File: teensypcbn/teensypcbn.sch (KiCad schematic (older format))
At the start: 10 parts, among them J1 CONN_26X2, J2 CONN_26X2, U1 Teensy4.1

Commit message: schema
schema voledig klaar
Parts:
- removed T?: HX1198FNLT, HX1198FNLT, symbol SamacSys_Parts:HX1198FNLT
- added C5, C6: 1000pF, Capacitor_SMD:C_0603_1608Metric_Pad0.99x1.00mm_HandSolder, symbol ESP32-PoE-ISO_Rev_C:Cap_Small
- added J4: SS-7188S-A-NF, SamacSys_Parts:SS-7188S-A-NF, symbol SamacSys_Parts:SS-7188S-A-NF
- added R1, R2, R3, R4: R_US, Resistor_SMD:R_0603_1608Metric, symbol Device:R_US
- added T1: HX1198FNLT, SamacSys_Parts:HX1198FNLT, symbol SamacSys_Parts:HX1198FNLT
- C1, C2, C3, C4: renamed from C?; footprint (none) -> Capacitor_SMD:C_0603_1608Metric_Pad0.99x1.00mm_HandSolder
- J3: renamed from J?; footprint 629104190121 -> SamacSys_Parts:629104190121
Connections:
- net RN: now also T1.8
- net RP: now also T1.6
- net TN: now also T1.3
- net TP: now also T1.1
- net at C1.1, C2.2: now also T1.2
- net at C3.1, C4.2: now also T1.7
- new net: R1.1, T1.10
- new net: J4.3, T1.11
- new net: J4.2, T1.14
- new net: R2.1, T1.15
- new net: J4.1, T1.16
- new net: J4.6, T1.9
- new net: J4.4, J4.5, R3.1
- new net: J4.7, J4.8, R4.1
- new net: C6.1, R3.2, R4.2
- new net: C5.1, R1.2, R2.2
- new net Earth: C5.2, C6.2
- no-connect marks 4 -> 6

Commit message: routing
routing begonnen
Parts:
- BT1: footprint Connector_JST:JST_PH_S2B-PH-SM4-TB_1x02-1MP_P2.00mm_Horizontal -> Connector_JST:JST_PH_B2B-PH-SM4-TB_1x02-1MP_P2.00mm_Vertical
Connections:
- net Earth is gone; now on net GND: C5.2, C6.2
- net R1P: now reaches J4.3, T1.11
- net T1N: now reaches J4.2, T1.14
- net T1P: now reaches J4.1, T1.16
- net R1N: now reaches J4.6, T1.9
- net LED0: no longer names the net of U1.61 (LED)
- no-connect marks 6 -> 7
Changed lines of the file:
@@
 F 0 "BT1" V 3975 770 50  0000 C CNN
 F 1 "Battery" V 4066 770 50  0000 C CNN
-F 2 "Connector_JST:JST_PH_S2B-PH-SM4-TB_1x02-1MP_P2.00mm_Horizontal" V 4220 830 50  0001 C CNN
+F 2 "Connector_JST:JST_PH_B2B-PH-SM4-TB_1x02-1MP_P2.00mm_Vertical" V 4220 830 50  0001 C CNN
 F 3 "~" V 4220 830 50  0001 C CNN
 	1    4220 770
@@
 Wire Wire Line
 	7490 4770 7970 4770
-Wire Wire Line
-	6970 4470 7210 4470
 $Comp
 L ESP32-PoE-ISO_Rev_C:Cap_Small C1
@@
 NoConn ~ 7970 4470
 NoConn ~ 7970 4370
-Text Label 7210 4470 2    50   ~ 0
-LED0
 Text Label 7085 4070 0    50   ~ 0
 TP
@@
 	9650 5620 9650 5290
 Connection ~ 9775 5620
-$Comp
-L power:Earth #PWR0105
-U 1 1 5F11E832
-P 9775 5810
-F 0 "#PWR0105" H 9775 5560 50  0001 C CNN
-F 1 "Earth" H 9775 5660 50  0001 C CNN
-F 2 "" H 9775 5810 50  0001 C CNN
-F 3 "~" H 9775 5810 50  0001 C CNN
-	1    9775 5810
-	1    0    0    -1
-$EndComp
 Wire Wire Line
 	9775 5810 9775 5720
@@
 	8990 5725 8990 5395
 Connection ~ 9115 5725
-$Comp
-L power:Earth #PWR0106
-U 1 1 5F1344FD
-P 9115 5915
-F 0 "#PWR0106" H 9115 5665 50  0001 C CNN
-F 1 "Earth" H 9115 5765 50  0001 C CNN
-F 2 "" H 9115 5915 50  0001 C CNN
-F 3 "~" H 9115 5915 50  0001 C CNN
-	1    9115 5915
-	1    0    0    -1
-$EndComp
 Wire Wire Line
 	9115 5915 9115 5825
@@
 Wire Wire Line
 	9915 4370 9665 4370
+Text Label 9125 4070 0    50   ~ 0
+T1P
+Text Label 9090 4270 0    50   ~ 0
+T1N
+Text Label 9085 4570 0    50   ~ 0
+R1P
+Text Label 9060 4770 0    50   ~ 0
+R1N
+$Comp
+L power:GND #PWR0106
+U 1 1 5F06739F
+P 9775 5810
+F 0 "#PWR0106" H 9775 5560 50  0001 C CNN
+F 1 "GND" H 9780 5637 50  0000 C CNN
+F 2 "" H 9775 5810 50  0001 C CNN
+F 3 "" H 9775 5810 50  0001 C CNN
+	1    9775 5810
+	1    0    0    -1
+$EndComp
+$Comp
+L power:GND #PWR0105
+U 1 1 5F0429FF
+P 9115 5915
+F 0 "#PWR0105" H 9115 5665 50  0001 C CNN
+F 1 "GND" H 9120 5742 50  0000 C CNN
+F 2 "" H 9115 5915 50  0001 C CNN
+F 3 "" H 9115 5915 50  0001 C CNN
+	1    9115 5915
+	1    0    0    -1
+$EndComp
+NoConn ~ 6970 4470
 $EndSCHEMATC

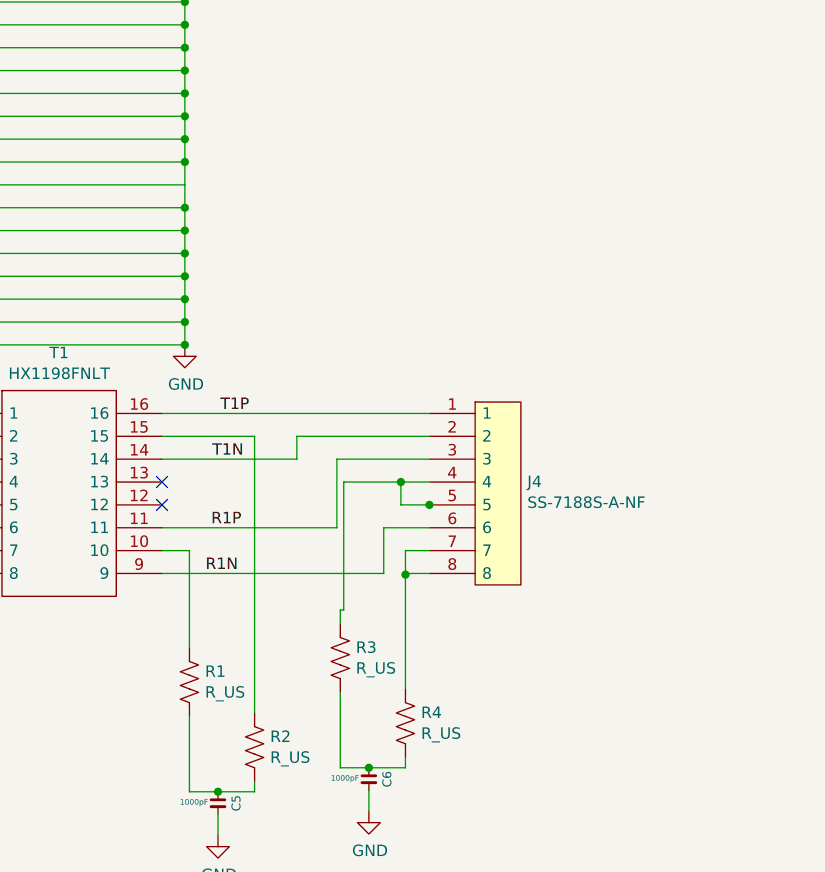
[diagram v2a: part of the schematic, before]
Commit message: routing V2
routing gestart met de juiste connector
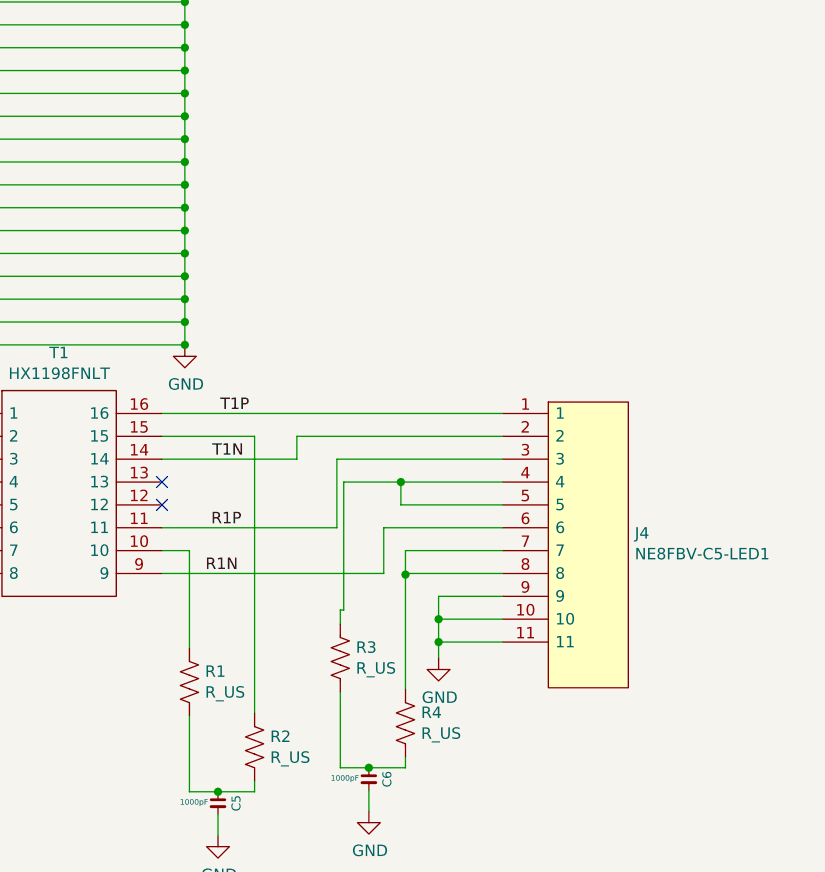
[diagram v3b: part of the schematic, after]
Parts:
- removed J4: SS-7188S-A-NF, SamacSys_Parts:SS-7188S-A-NF, symbol SamacSys_Parts:SS-7188S-A-NF
- added J4: NE8FBV-C5-LED1, SamacSys_Parts:NE8FBVC5LED1, symbol SamacSys_Parts:NE8FBV-C5-LED1
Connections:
- net GND: now also J2.15, J4.10, J4.11, J4.9
- net R1N: now also J4.6
- net R1P: now also J4.3
- net T1N: now also J4.2
- net T1P: now also J4.1
- net at R3.1: now also J4.4, J4.5
- net at R4.1: now also J4.7, J4.8
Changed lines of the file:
@@
 	8100 3170 8970 3170
 Wire Wire Line
-	8970 3270 8970 3170
-Connection ~ 8970 3170
-Wire Wire Line
 	8100 2970 8970 2970
-Wire Wire Line
-	8970 3170 8970 2970
-Connection ~ 8970 2970
 Wire Wire Line
 	8100 2870 8970 2870
@@
 Wire Wire Line
 	7970 4670 7970 4710
-$Comp
-L SamacSys_Parts:SS-7188S-A-NF J4
-U 1 1 5F04A257
-P 10240 4370
-F 0 "J4" H 10468 4371 50  0000 L CNN
-F 1 "SS-7188S-A-NF" H 10468 4280 50  0000 L CNN
-F 2 "SamacSys_Parts:SS-7188S-A-NF" H 10490 4620 50  0001 L CNN
-F 3 "" H 10490 4520 50  0001 L CNN
-F 4 "Bel-Stewart Cat5e RJ45 Connector Socket, Shielded, Right Angle, Through Hole" H 10490 4420 50  0001 L CNN "Description"
-F 5 "530-SS-7188S-A-NF" H 10490 4220 50  0001 L CNN "Mouser Part Number"
-F 6 "https://www.mouser.co.uk/ProductDetail/Stewart-Connector-Bel/SS-7188S-A-NF?qs=FESYatJ8odJ%252BI%2FN%2FnbWjsA%3D%3D" H 10490 4120 50  0001 L CNN "Mouser Price/Stock"
-F 7 "Bel-Stewart" H 10490 4020 50  0001 L CNN "Manufacturer_Name"
-F 8 "SS-7188S-A-NF" H 10490 3920 50  0001 L CNN "Manufacturer_Part_Number"
-	1    10240 4370
-	1    0    0    -1
-$EndComp
-Wire Wire Line
-	8870 4070 10040 4070
 Wire Wire Line
 	8870 4270 9460 4270
 Wire Wire Line
 	9460 4270 9460 4170
-Wire Wire Line
-	9460 4170 10040 4170
 NoConn ~ 8870 4370
 NoConn ~ 8870 4470
@@
 	9635 4570 9635 4270
 Wire Wire Line
-	9635 4270 10040 4270
-Wire Wire Line
 	8870 4770 9840 4770
 Wire Wire Line
 	9840 4770 9840 4570
-Wire Wire Line
-	9840 4570 10040 4570
 $Comp
 L Device:R_US R3
@@
 $EndComp
 Wire Wire Line
-	10040 4670 9935 4670
-Wire Wire Line
 	9935 4670 9935 4775
-Wire Wire Line
-	10040 4770 9940 4770
 Wire Wire Line
 	9940 4770 9940 4775
@@
 	9275 4170 9275 5380
 Wire Wire Line
-	10040 4370 9915 4370
-Wire Wire Line
 	9665 4370 9665 4930
 Wire Wire Line
@@
 	9650 4930 9650 4990
 Wire Wire Line
-	10045 4470 10040 4470
-Wire Wire Line
 	9915 4470 9915 4370
-Connection ~ 10040 4470
-Wire Wire Line
-	10040 4470 9915 4470
 Connection ~ 9915 4370
 Wire Wire Line
@@
 $EndComp
 NoConn ~ 6970 4470
+Wire Wire Line
+	8970 2970 8970 3070
+Connection ~ 8970 2970
+Wire Wire Line
+	8970 3070 8970 3170
+Connection ~ 8970 3070
+Connection ~ 8970 3170
+Wire Wire Line
+	8970 3170 8970 3270
+$Comp
+L power:GND #PWR0107
+U 1 1 5F0723BF
+P 10080 5140
+F 0 "#PWR0107" H 10080 4890 50  0001 C CNN
+F 1 "GND" H 10085 4967 50  0000 C CNN
+F 2 "" H 10080 5140 50  0001 C CNN
+F 3 "" H 10080 5140 50  0001 C CNN
+	1    10080 5140
+	1    0    0    -1
+$EndComp
+Wire Wire Line
+	9940 4770 10360 4770
+Wire Wire Line
+	9935 4670 10360 4670
+Wire Wire Line
+	8870 4070 10360 4070
+Wire Wire Line
+	9460 4170 10360 4170
+Wire Wire Line
+	9635 4270 10360 4270
+Wire Wire Line
+	9915 4370 10360 4370
+$Comp
+L SamacSys_Parts:NE8FBV-C5-LED1 J4
+U 1 1 5F0E1554
+P 10360 4070
+F 0 "J4" H 10938 3546 50  0000 L CNN
+F 1 "NE8FBV-C5-LED1" H 10938 3455 50  0000 L CNN
+F 2 "SamacSys_Parts:NE8FBVC5LED1" V 10860 3020 50  0001 L CNN
+F 3 "" H 9760 3520 50  0001 L CNN
+F 4 "28.7" H 10710 2920 50  0001 L CNN "Height"
+	1    10360 4070
+	1    0    0    -1
+$EndComp
+Wire Wire Line
+	9915 4470 10360 4470
+Wire Wire Line
+	9840 4570 10360 4570
+Wire Wire Line
+	10080 4870 10360 4870
+Wire Wire Line
+	10360 4970 10080 4970
+Connection ~ 10080 4970
+Wire Wire Line
+	10080 4970 10080 4870
+Wire Wire Line
+	10360 5070 10080 5070
+Wire Wire Line
+	10080 4970 10080 5070
+Connection ~ 10080 5070
+Wire Wire Line
+	10080 5070 10080 5140
 $EndSCHEMATC

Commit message: placment
placment bijna klaar
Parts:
- removed J4: NE8FBV-C5-LED1, SamacSys_Parts:NE8FBVC5LED1, symbol SamacSys_Parts:NE8FBV-C5-LED1
- added J4: NE8FAH-C5, SamacSys_Parts:NE8FAHC5, symbol SamacSys_Parts:NE8FAH-C5
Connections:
- net GND: now also J4.G1
- net R1N: now also J4.6
- net R1P: now also J4.3
- net T1N: now also J4.2
- net T1P: now also J4.1
- net at R3.1: now also J4.4, J4.5
- net at R4.1: now also J4.7, J4.8
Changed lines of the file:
@@
 Wire Wire Line
 	9915 4370 10360 4370
-$Comp
-L SamacSys_Parts:NE8FBV-C5-LED1 J4
-U 1 1 5F0E1554
-P 10360 4070
-F 0 "J4" H 10938 3546 50  0000 L CNN
-F 1 "NE8FBV-C5-LED1" H 10938 3455 50  0000 L CNN
-F 2 "SamacSys_Parts:NE8FBVC5LED1" V 10860 3020 50  0001 L CNN
-F 3 "" H 9760 3520 50  0001 L CNN
-F 4 "28.7" H 10710 2920 50  0001 L CNN "Height"
-	1    10360 4070
-	1    0    0    -1
-$EndComp
 Wire Wire Line
 	9915 4470 10360 4470
@@
 Wire Wire Line
 	10080 4870 10360 4870
+$Comp
+L SamacSys_Parts:NE8FAH-C5 J4
+U 1 1 5F148EB7
+P 10360 4070
+F 0 "J4" H 10738 3691 50  0000 L CNN
+F 1 "NE8FAH-C5" H 10738 3600 50  0000 L CNN
+F 2 "SamacSys_Parts:NE8FAHC5" H 10760 3320 50  0001 L CNN
+F 3 "https://www.neutrik.com/media/10049/download/ne8fah-c5-1.pdf?v=1" H 10760 3420 50  0001 L CNN
+F 4 "NEUTRIK - NE8FAH-C5 - CONNECTOR, RJ45, JACK, 8P8C, CAT5E" H 10760 3520 50  0001 L CNN "Description"
+F 5 "28.7" H 10510 3470 50  0001 L CNN "Height"
+F 6 "568-NE8FAH-C5" H 10760 3720 50  0001 L CNN "Mouser Part Number"
+F 7 "https://www.mouser.co.uk/ProductDetail/Neutrik/NE8FAH-C5?qs=yAJ577jGV73mSHthIeMdNw%3D%3D" H 10760 3820 50  0001 L CNN "Mouser Price/Stock"
+F 8 "Neutrik" H 10760 3920 50  0001 L CNN "Manufacturer_Name"
+F 9 "NE8FAH-C5" H 10760 4020 50  0001 L CNN "Manufacturer_Part_Number"
+	1    10360 4070
+	1    0    0    -1
+$EndComp
 Wire Wire Line
-	10360 4970 10080 4970
-Connection ~ 10080 4970
-Wire Wire Line
-	10080 4970 10080 4870
-Wire Wire Line
-	10360 5070 10080 5070
-Wire Wire Line
-	10080 4970 10080 5070
-Connection ~ 10080 5070
-Wire Wire Line
-	10080 5070 10080 5140
+	10080 4870 10080 5140
 $EndSCHEMATC

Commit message: routing klaar
routing klaar , bom moet nog aangepast worden
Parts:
- C1, C2, C3, C4: value 0.1 -> 0.1uF
- R1, R2, R3, R4: value R_US -> 75ohm
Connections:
- net GND: now also J1.15
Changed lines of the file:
@@
 Wire Wire Line
 	3440 2070 2570 2070
-Wire Wire Line
-	2570 1870 2570 2070
 Connection ~ 2570 2070
 Wire Wire Line
 	3440 2170 2570 2170
-Wire Wire Line
-	2570 1970 3440 1970
 Wire Wire Line
 	2570 2070 2570 2170
@@
 U 1 1 5F115703
 P 3275 4570
-F 0 "J3" H 4133 5035 50  0000 C CNN
-F 1 "629104190121" H 4133 4944 50  0000 C CNN
+F 0 "J3" V 3350 4745 50  0000 C CNN
+F 1 "629104190121" V 3235 4760 50  0000 C CNN
 F 2 "SamacSys_Parts:629104190121" H 4225 4670 50  0001 L CNN
 F 3 "http://katalog.we-online.de/em/datasheet/629104190121.pdf" H 4225 4570 50  0001 L CNN
@@
 P 7795 4120
 F 0 "C1" V 7760 4065 39  0000 C CNN
-F 1 "0.1" V 7775 4175 24  0000 C CNN
+F 1 "0.1uF" V 7770 4195 24  0000 C CNN
 F 2 "Capacitor_SMD:C_0603_1608Metric_Pad0.99x1.00mm_HandSolder" H 7795 4120 60  0001 C CNN
 F 3 "" H 7795 4120 60  0000 C CNN
@@
 P 7795 4200
 F 0 "C2" V 7820 4145 39  0000 C CNN
-F 1 "0.1" V 7770 4145 24  0000 C CNN
+F 1 "0.1uF" V 7770 4125 24  0000 C CNN
 F 2 "Capacitor_SMD:C_0603_1608Metric_Pad0.99x1.00mm_HandSolder" H 7795 4200 60  0001 C CNN
 F 3 "" H 7795 4200 60  0000 C CNN
@@
 P 7835 4630
 F 0 "C3" V 7800 4575 39  0000 C CNN
-F 1 "0.1" V 7815 4685 24  0000 C CNN
+F 1 "0.1uF" V 7815 4710 24  0000 C CNN
 F 2 "Capacitor_SMD:C_0603_1608Metric_Pad0.99x1.00mm_HandSolder" H 7835 4630 60  0001 C CNN
 F 3 "" H 7835 4630 60  0000 C CNN
@@
 P 7835 4710
 F 0 "C4" V 7860 4655 39  0000 C CNN
-F 1 "0.1" V 7810 4655 24  0000 C CNN
+F 1 "0.1uF" V 7810 4630 24  0000 C CNN
 F 2 "Capacitor_SMD:C_0603_1608Metric_Pad0.99x1.00mm_HandSolder" H 7835 4710 60  0001 C CNN
 F 3 "" H 7835 4710 60  0000 C CNN
@@
 P 9650 5140
 F 0 "R3" H 9718 5186 50  0000 L CNN
-F 1 "R_US" H 9718 5095 50  0000 L CNN
+F 1 "75ohm" V 9570 5015 50  0000 L CNN
 F 2 "Resistor_SMD:R_0603_1608Metric" V 9690 5130 50  0001 C CNN
 F 3 "~" H 9650 5140 50  0001 C CNN
@@
 U 1 1 5F0FEAAA
 P 9935 5425
-F 0 "R4" H 10003 5471 50  0000 L CNN
-F 1 "R_US" H 10003 5380 50  0000 L CNN
+F 0 "R4" V 10015 5380 50  0000 L CNN
+F 1 "75ohm" V 9860 5315 50  0000 L CNN
 F 2 "Resistor_SMD:R_0603_1608Metric" V 9975 5415 50  0001 C CNN
 F 3 "~" H 9935 5425 50  0001 C CNN
@@
 P 8990 5245
 F 0 "R1" H 9058 5291 50  0000 L CNN
-F 1 "R_US" H 9058 5200 50  0000 L CNN
+F 1 "75ohm" V 8900 5115 50  0000 L CNN
 F 2 "Resistor_SMD:R_0603_1608Metric" V 9030 5235 50  0001 C CNN
 F 3 "~" H 8990 5245 50  0001 C CNN
@@
 P 9275 5530
 F 0 "R2" H 9343 5576 50  0000 L CNN
-F 1 "R_US" H 9343 5485 50  0000 L CNN
+F 1 "75ohm" V 9205 5435 50  0000 L CNN
 F 2 "Resistor_SMD:R_0603_1608Metric" V 9315 5520 50  0001 C CNN
 F 3 "~" H 9275 5530 50  0001 C CNN
@@
 Wire Wire Line
 	10080 4870 10080 5140
+Wire Wire Line
+	3440 1970 2570 1970
+Wire Wire Line
+	2570 1870 2570 1970
+Connection ~ 2570 1970
+Wire Wire Line
+	2570 1970 2570 2070
 $EndSCHEMATC
